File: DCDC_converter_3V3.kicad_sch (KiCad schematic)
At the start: 24 parts, among them J6 DC barrel assy, J8 Dell DC jack, U1 LMR380x0

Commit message: sch update
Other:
- note added: "Return to front sheet"
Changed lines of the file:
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@@
+		)
+	)
+	(text "Return to front sheet"
+		(exclude_from_sim no)
+		(at 12.7 197.485 0)
+		(effects
+			(font
+				(face "DejaVu Sans")
+				(size 2.032 2.032)
+				(thickness 0.3175)
+				(color 0 0 0 1)
+			)
+			(justify left bottom)
+			(href "#1")
 		)
 	)

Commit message: reorganised sch and pcb
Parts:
- J6: Assy (none) -> ${REFERENCE}
- J8: BarrelConn (none) -> ${REFERENCE}
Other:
- note added: "is fitted to a small "standalone" PCB which will then be soldered into the "main" PCB. This standalone PCB + connector are what make the "DC barrel assy" used in position."
- moved on the sheet: J8
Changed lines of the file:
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@@
 	(paper "A4")
 	(rectangle
+		(start 25.4 114.3)
+		(end 63.5 152.4)
+		(stroke
+			(width 0.254)
+			(type dash)
+			(color 0 0 0 1)
+		)
+		(fill
+			(type none)
+		)
+	)
+	(rectangle
 		(start 13.97 13.97)
 		(end 48.26 31.75)
@@
 		)
 	)
+	(text "    is fitted to a small \"standalone\" PCB which\nwill then be soldered into the \"main\" PCB.\nThis standalone PCB + connector are what make\nthe \"DC barrel assy\" used in     position."
+		(exclude_from_sim no)
+		(at 25.4 154.305 0)
+		(effects
+			(font
+				(size 2.032 2.032)
+				(color 0 0 0 1)
+			)
+			(justify left top)
+		)
+	)
 	(text "Return to front sheet"
 		(exclude_from_sim no)
@@
 	)
 	(junction
-		(at 54.61 135.89)
+		(at 54.61 139.7)
 		(diameter 0)
 		(color 0 0 0 0)
@@
 	)
 	(no_connect
-		(at 50.8 130.81)
+		(at 50.8 134.62)
 	)
 	(wire
@@
 	(wire
 		(pts
-			(xy 50.8 133.35) (xy 54.61 133.35)
+			(xy 50.8 137.16) (xy 54.61 137.16)
 		)
 		(stroke
@@
 	(wire
 		(pts
-			(xy 54.61 133.35) (xy 54.61 135.89)
+			(xy 54.61 137.16) (xy 54.61 139.7)
 		)
 		(stroke
@@
 	(wire
 		(pts
-			(xy 54.61 135.89) (xy 54.61 137.16)
+			(xy 54.61 139.7) (xy 54.61 140.97)
 		)
 		(stroke
@@
 	(wire
 		(pts
-			(xy 54.61 128.27) (xy 54.61 127)
+			(xy 54.61 132.08) (xy 54.61 130.81)
 		)
 		(stroke
@@
 	(wire
 		(pts
-			(xy 50.8 128.27) (xy 54.61 128.27)
+			(xy 50.8 132.08) (xy 54.61 132.08)
 		)
 		(stroke
@@
 	(wire
 		(pts
-			(xy 50.8 135.89) (xy 54.61 135.89)
+			(xy 50.8 139.7) (xy 54.61 139.7)
 		)
 		(stroke
@@
 	(symbol
 		(lib_id "personal:Cosmetic_PWR_SRC")
-		(at 54.61 127 0)
+		(at 54.61 130.81 0)
 		(unit 1)
 		(body_style 1)
@@
 		(fields_autoplaced yes)
 		(property "Reference" "Pwr014"
-			(at 54.61 122.682 0)
+			(at 54.61 126.492 0)
 			(hide yes)
 			(show_name no)
@@
 		)
 		(property "Value" "S19V5_2"
-			(at 54.61 122.936 0)
+			(at 54.61 126.746 0)
 			(show_name no)
 			(do_not_autoplace yes)
@@
 		)
 		(property "Footprint" ""
-			(at 54.61 127 0)
+			(at 54.61 130.81 0)
 			(hide yes)
 			(show_name no)
@@
 		)
 		(property "Datasheet" ""
-			(at 54.61 127 0)
+			(at 54.61 130.81 0)
 			(hide yes)
 			(show_name no)
@@
 		)
 		(property "Description" "Local power symbol (source), cosmetic use only"
-			(at 54.61 127 0)
+			(at 54.61 130.81 0)
 			(hide yes)
 			(show_name no)
@@
 	(symbol
 		(lib_id "personal:Cosmetic_GND")
-		(at 54.61 137.16 0)
+		(at 54.61 140.97 0)
 		(unit 1)
 		(body_style 1)
@@
 		(fields_autoplaced yes)
 		(property "Reference" "Pwr017"
-			(at 54.61 132.842 0)
+			(at 54.61 136.652 0)
 			(hide yes)
 			(show_name no)
@@
 		)
 		(property "Value" "GND_2"
-			(at 54.61 140.716 0)
+			(at 54.61 144.526 0)
 			(show_name no)
 			(do_not_autoplace yes)
@@
 		)
 		(property "Footprint" ""
-			(at 54.61 137.16 0)
+			(at 54.61 140.97 0)
 			(hide yes)
 			(show_name no)
@@
 		)
 		(property "Datasheet" ""
-			(at 54.61 137.16 0)
+			(at 54.61 140.97 0)
 			(hide yes)
 			(show_name no)
@@
 		)
 		(property "Description" "Local power symbol (sink), cosmetic use only"
-			(at 54.61 137.16 0)
+			(at 54.61 140.97 0)
 			(hide yes)
 			(show_name no)
@@
 		(in_pos_files yes)
 		(dnp no)
-		(fields_autoplaced yes)
 		(property "Reference" "J6"
 			(at 36.322 70.612 0)
@@
 			)
 		)
+		(property "Assy" "${REFERENCE}"
+			(at 67.945 165.1 0)
+			(show_name no)
+			(do_not_autoplace no)
+			(effects
+				(font
+					(size 2.032 2.032)
+				)
+			)
+		)
 		(pin "2"
 		)
@@
 	(symbol
 		(lib_id "personal:Dell_DC_barrel_jack")
-		(at 43.18 132.08 0)
+		(at 43.18 135.89 0)
 		(unit 1)
 		(body_style 1)
@@
 		(in_pos_files yes)
 		(dnp no)
-		(fields_autoplaced yes)
 		(property "Reference" "J8"
-			(at 37.592 123.952 0)
+			(at 37.592 127.762 0)
 			(show_name no)
 			(do_not_autoplace yes)
@@
 		)
 		(property "Value" "Dell DC jack"
-			(at 37.592 125.73 0)
+			(at 37.592 129.54 0)
 			(show_name no)
 			(do_not_autoplace yes)
@@
 		)
 		(property "Footprint" "Personal:Dell DC jack"
-			(at 43.18 132.08 0)
+			(at 43.18 135.89 0)
 			(hide yes)
 			(show_name no)
@@
 		)
 		(property "Datasheet" ""
-			(at 43.18 132.08 0)
+			(at 43.18 135.89 0)
 			(hide yes)
 			(show_name no)
@@
 		)
 		(property "Description" ""
-			(at 43.18 132.08 0)
+			(at 43.18 135.89 0)
 			(hide yes)
 			(show_name no)
@@
 				)
 			)
+		)
+		(property "BarrelConn" "${REFERENCE}"
+			(at 26.67 154.94 0)
+			(show_name no)
+			(do_not_autoplace no)
+			(effects
+				(font
+					(size 2.032 2.032)
+				)
+			)

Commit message: updated sch template (A4)
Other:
- note removed: "${SHEETNAME}"
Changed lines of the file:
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@@
 				(size 2.032 2.032)
 				(thickness 0.3175)
-				(color 0 0 0 1)
+				(color 0 0 194 1)
 			)
 			(justify left bottom)
@@
 		)
 	)
-	(text "${SHEETNAME}"
-		(exclude_from_sim no)
-		(at 283.21 14.605 0)
-		(effects
-			(font
-				(face "DejaVu Sans")
-				(size 3.81 3.81)
-				(bold yes)
-				(color 0 0 0 1)
-			)
-			(justify right top)
-		)
-	)

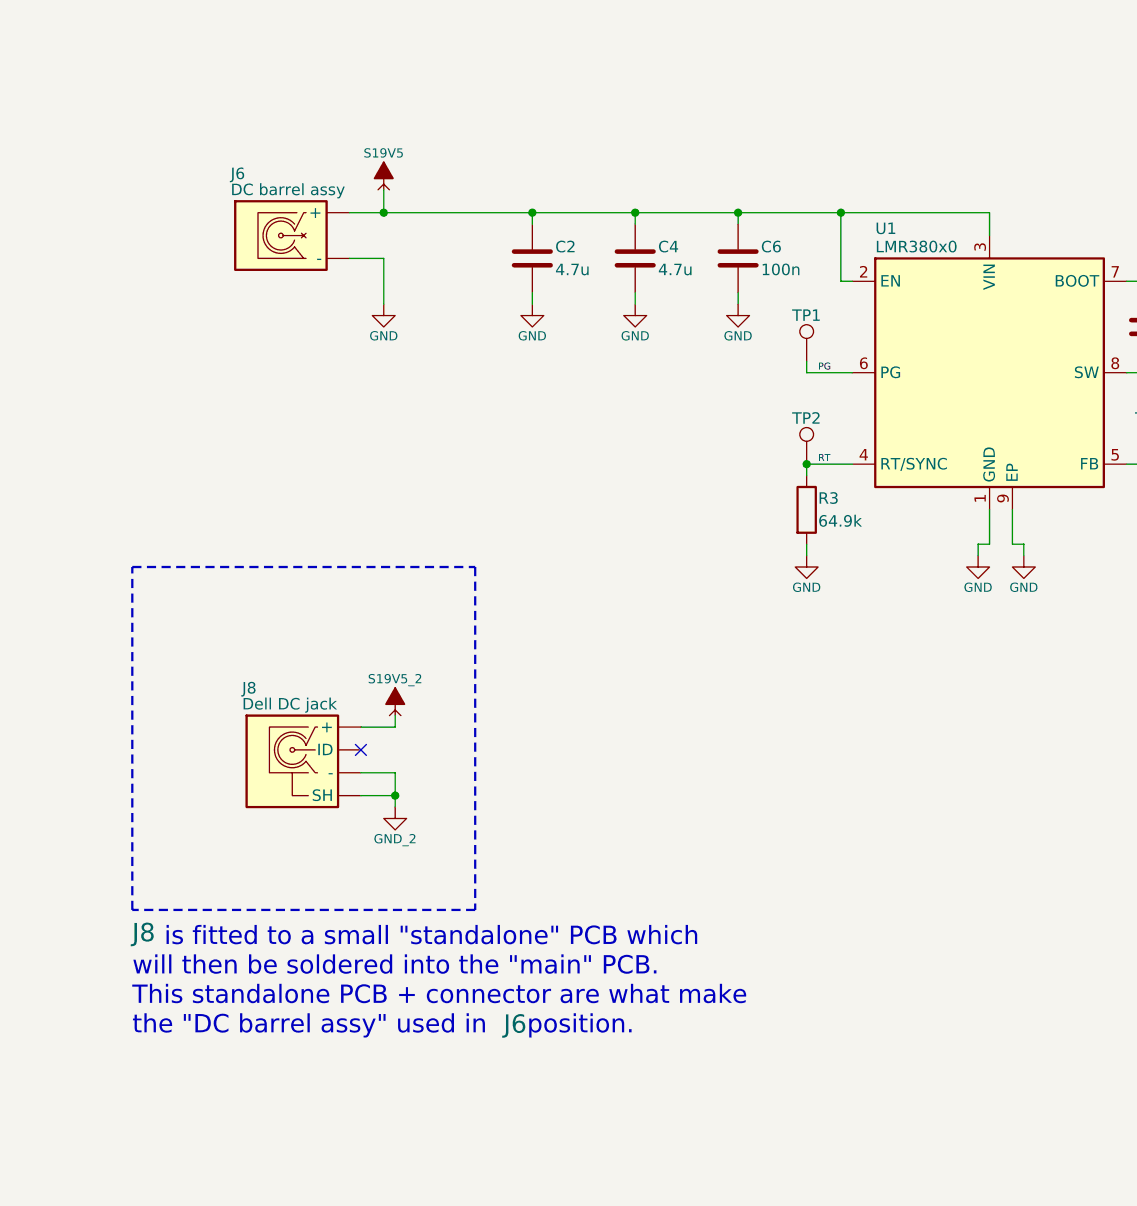
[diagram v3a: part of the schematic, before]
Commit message: supplier and mpn added
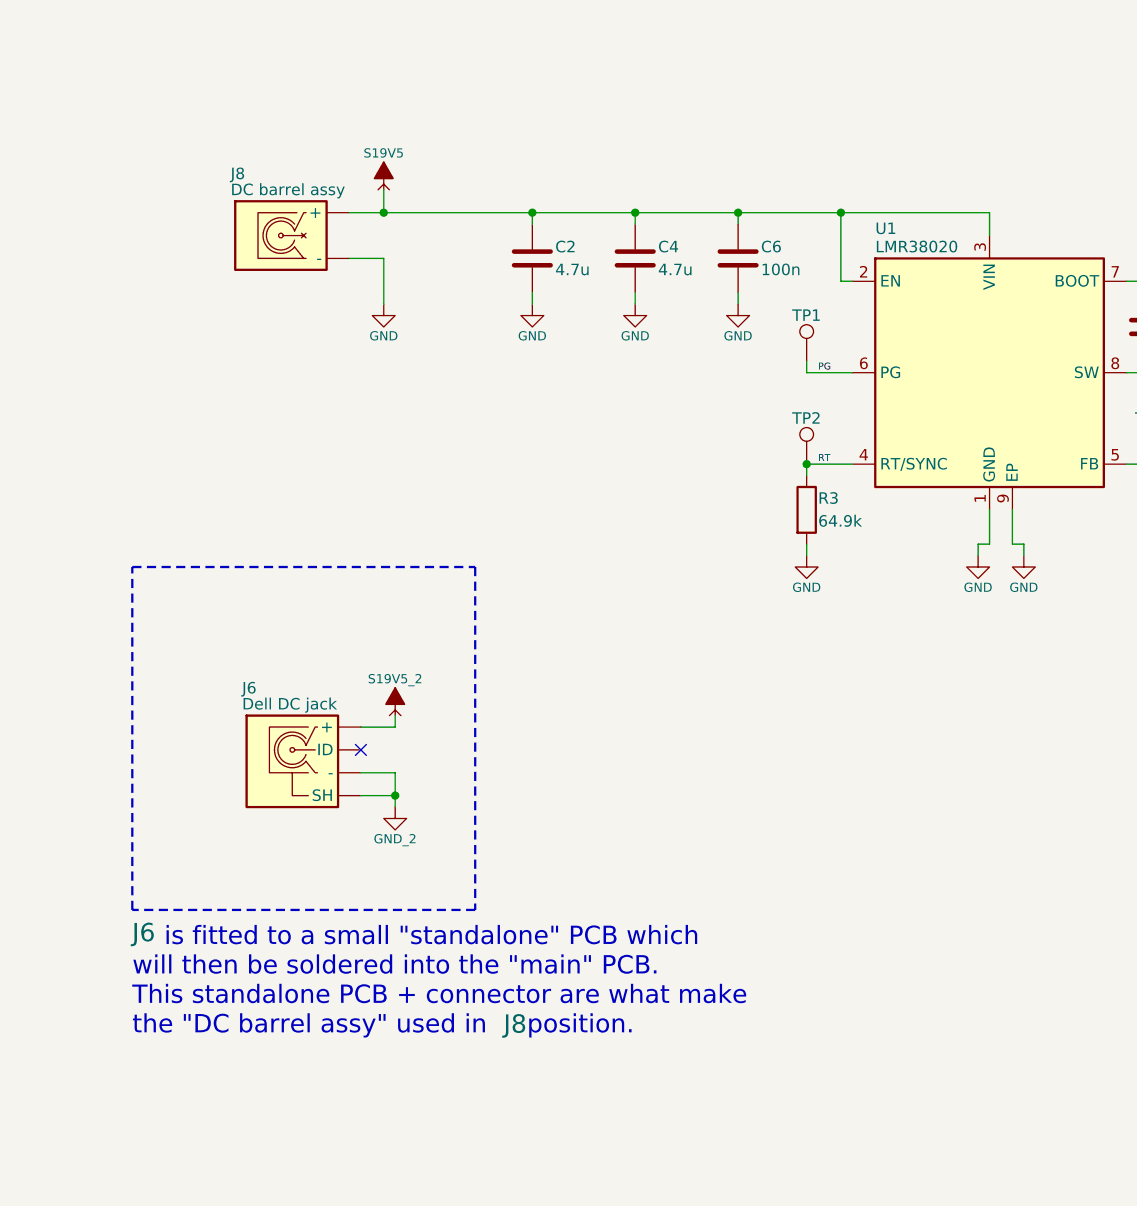
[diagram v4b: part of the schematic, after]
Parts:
- C12: Manufacturer (none) -> Yageo; Manufacturer Part Number (none) -> AC0603JRNPO9BN330
- C15, C17, C18: Manufacturer (none) -> TAIYO YUDEN; Manufacturer Part Number (none) -> MCAST32MSB7226KPNA01
- C2, C4: Manufacturer (none) -> KEMET; Manufacturer Part Number (none) -> C1206C475K5RACAUTO
- C6, C9: Manufacturer (none) -> Yageo; Manufacturer Part Number (none) -> AC0603KRX7R9BB104
- J6: renamed from J8; Manufacturer (none) -> Dell; Manufacturer Part Number (none) -> Barrel jack
- J8: renamed from J6; Manufacturer (none) -> NA; Manufacturer Part Number (none) -> NA
- L1: Manufacturer (none) -> Bourns; Manufacturer Part Number (none) -> SRP6540-100M
- R3: Manufacturer (none) -> YAGEO; Manufacturer Part Number (none) -> AC0603FR-0764K9L
- R6: Manufacturer (none) -> YAGEO; Manufacturer Part Number (none) -> AC0603FR-0723K2L
- R7: Manufacturer (none) -> YAGEO; Manufacturer Part Number (none) -> AC0603FR-0710KL
- TP1, TP18, TP2, TP5, TP6, TP7: Manufacturer (none) -> NA; Manufacturer Part Number (none) -> NA; now left out of the parts list
- TP10: renamed from TP17; Manufacturer (none) -> NA; Manufacturer Part Number (none) -> NA; now left out of the parts list
- TP17: renamed from TP10; Manufacturer (none) -> NA; Manufacturer Part Number (none) -> NA; now left out of the parts list
- U1: value LMR380x0 -> LMR38020; Manufacturer (none) -> Texas instruments; Manufacturer Part Number (none) -> LMR38020FDDAR
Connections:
- net 3V3_REG: now also TP10.1; no longer TP17.1
- net S3V3: now also TP17.1; no longer TP10.1
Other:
- moved on the sheet: TP10, TP17

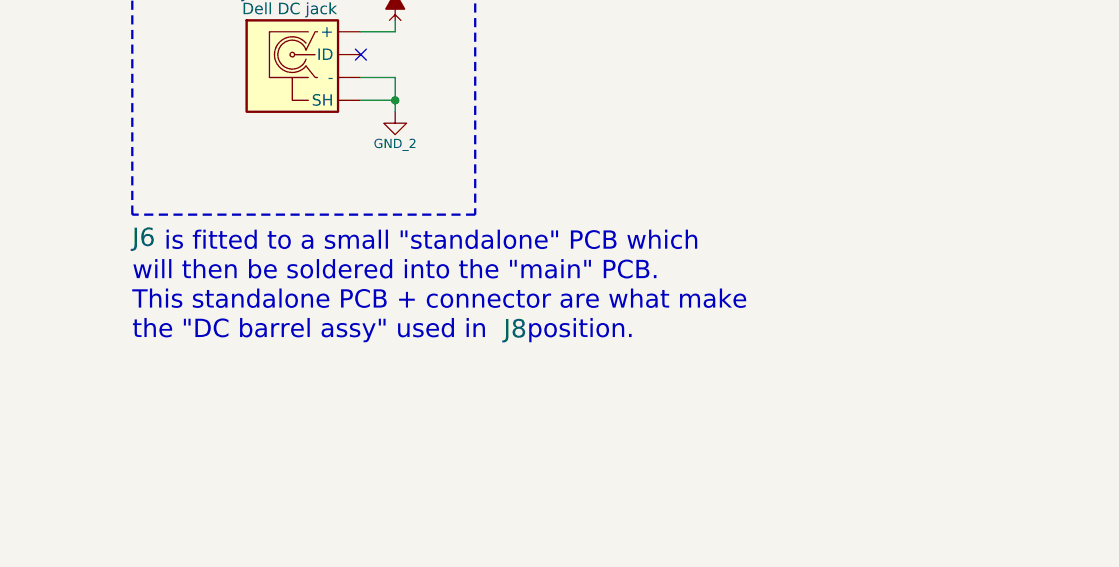
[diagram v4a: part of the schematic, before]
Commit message: added lib tables
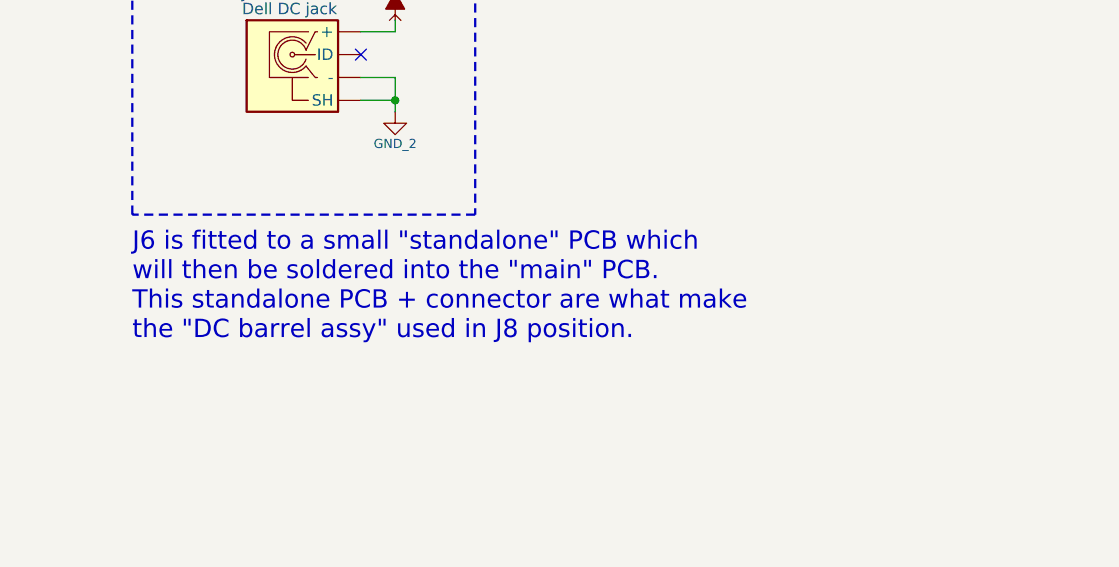
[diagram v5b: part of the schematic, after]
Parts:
- J6: BarrelConn ${REFERENCE} -> (none)
- J8: Assy ${REFERENCE} -> (none)
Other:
- note added: "J6 is fitted to a small "standalone" PCB which will then be soldered into the "main" PCB. This standalone PCB + connector are what make the "DC barrel assy" used in J8 position."
- note removed: "is fitted to a small "standalone" PCB which will then be soldered into the "main" PCB. This standalone PCB + connector are what make the "DC barrel assy" used in position."
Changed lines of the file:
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@@
 	(generator_version "10.0")
 	(paper "A4")
+	(title_block
+		(date "2026-10-06")
+		(rev "1.0.1")
+	)
 	(rectangle
 		(start 25.4 114.3)
@@
 		)
 	)
-	(text "    is fitted to a small \"standalone\" PCB which\nwill then be soldered into the \"main\" PCB.\nThis standalone PCB + connector are what make\nthe \"DC barrel assy\" used in     position."
+	(text "J6 is fitted to a small \"standalone\" PCB which\nwill then be soldered into the \"main\" PCB.\nThis standalone PCB + connector are what make\nthe \"DC barrel assy\" used in J8 position."
 		(exclude_from_sim no)
 		(at 25.4 154.305 0)
@@
 			)
 		)
-		(property "Assy" "${REFERENCE}"
-			(at 67.945 165.1 0)
-			(show_name no)
-			(do_not_autoplace no)
-			(effects
-				(font
-					(size 2.032 2.032)
-				)
-			)
-		)
 		(property "Manufacturer" "NA"
 			(at 41.91 77.47 0)
@@
 				)
 			)
-		)
-		(property "BarrelConn" "${REFERENCE}"
-			(at 26.67 154.94 0)
-			(show_name no)
-			(do_not_autoplace no)
-			(effects
-				(font
-					(size 2.032 2.032)
-				)
-			)
